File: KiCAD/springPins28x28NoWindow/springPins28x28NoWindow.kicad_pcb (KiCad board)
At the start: 2 copper layers, 28 x 28 mm, 26 parts, among them J1 CONN_02X06, J2 CONN_02X06

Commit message: update silk
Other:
- board text added: "c75b306"
- board text removed: "1ad7c5f"
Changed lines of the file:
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@@
     (effects (font (size 1 1) (thickness 0.25)))
   )
-  (gr_text 1ad7c5f (at 6.5 -12.5) (layer F.SilkS)
+  (gr_text c75b306 (at 6.5 -12.5) (layer F.SilkS)
     (effects (font (size 0.7 0.7) (thickness 0.175)))
   )

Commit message: wip commit
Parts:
- moved JP1 22.9 mm to (-5.50, -11.1)
- moved R1 13.7 mm to (5.00, 1.00), turned to 0 degrees
- moved J1 12.7 mm to (6.35, 6.35), turned to 90 degrees
- moved J2 10.5 mm to (6.35, -3.81), turned to 90 degrees
- moved G*** 10.2 mm to (0.00, 10.2), turned to 180 degrees
- turned L1 to 0 degrees
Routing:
- net /V5: track 6.21 -> 29.3 mm, vias 0 -> 1
- net /I5: track 6.40 -> 21.9 mm
- net /V3: track 7.00 -> 22.4 mm
- net /I7: track 9.29 -> 24.0 mm
- net /I3: track 7.20 -> 21.9 mm
- net /V1: track 7.80 -> 22.3 mm
- net /I2: track 7.99 -> 21.5 mm
- net /I1: track 7.99 -> 20.7 mm
- net /V2: track 7.80 -> 16.9 mm
- net /I6: track 6.40 -> 15.3 mm
- net /I4: track 7.20 -> 15.3 mm
- net /V7: track 15.2 -> 22.8 mm
- net /V6: track 6.21 -> 13.7 mm
- net /V4: track 7.00 -> 13.9 mm
- net /I8: track 9.29 -> 15.2 mm
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
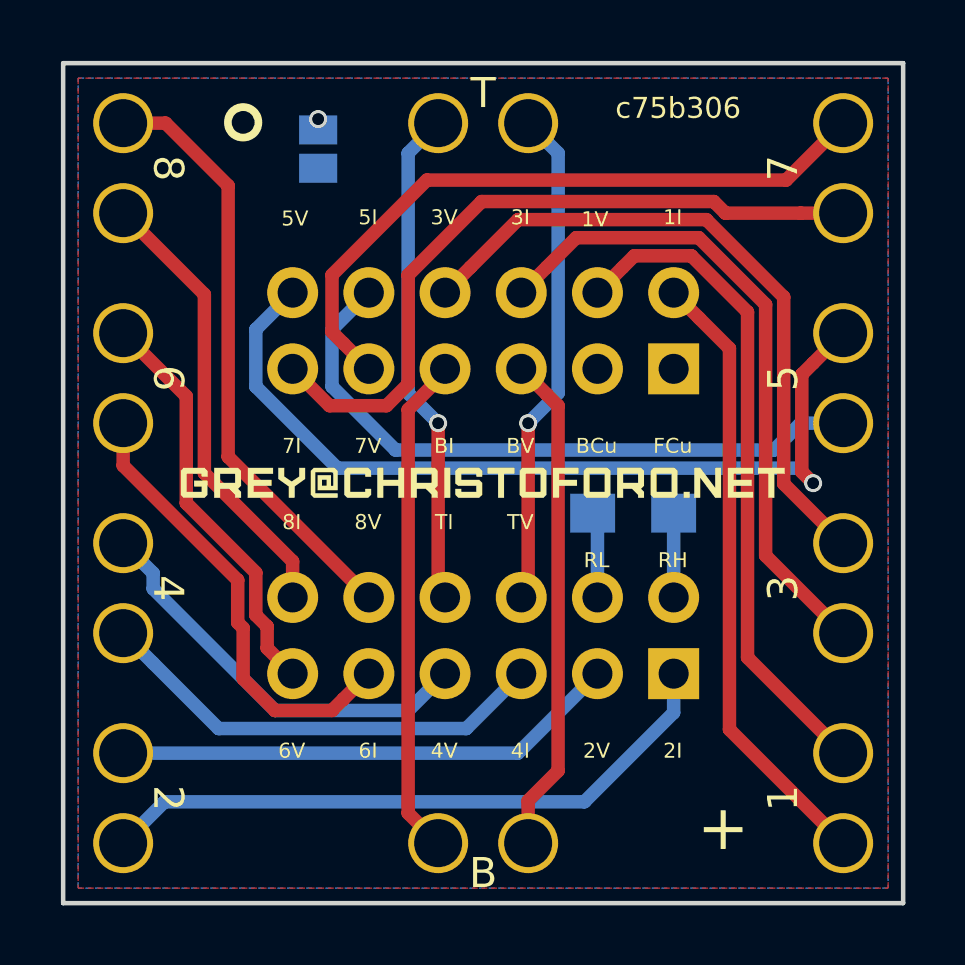
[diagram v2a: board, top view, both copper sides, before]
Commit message: go back to 28x28 layout
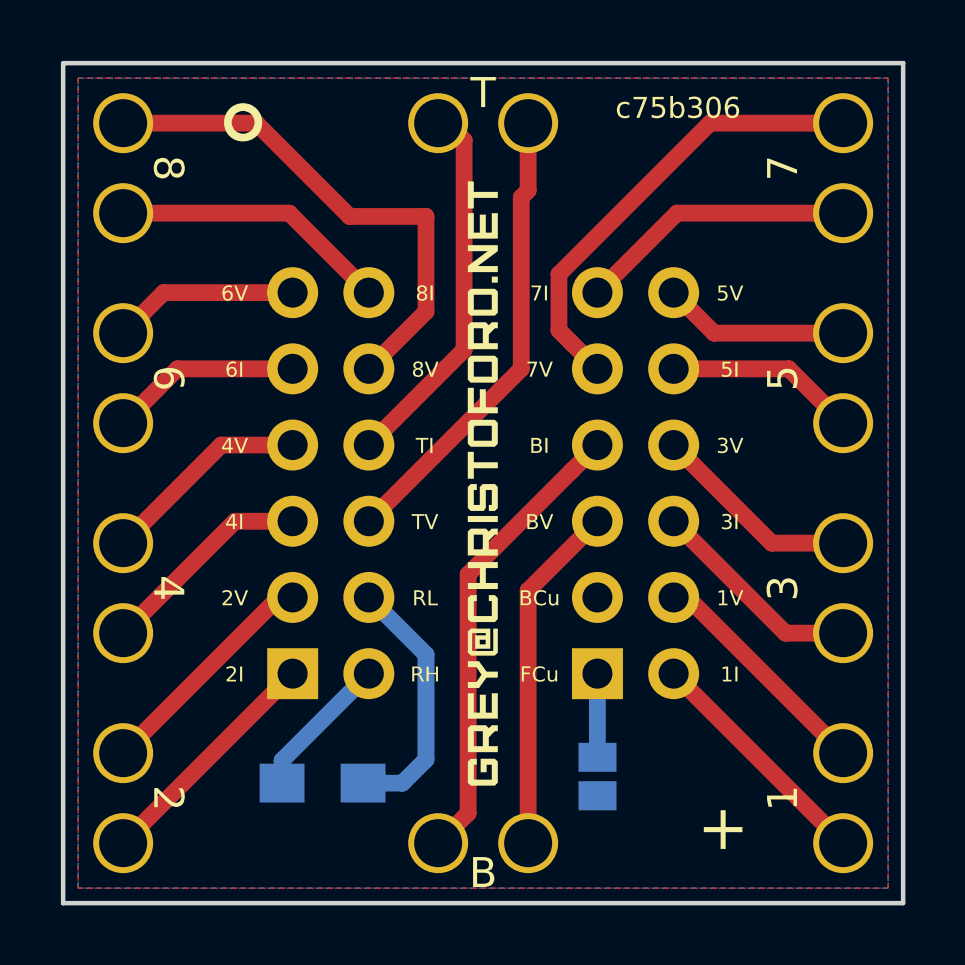
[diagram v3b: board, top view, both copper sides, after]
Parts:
- moved JP1 22.9 mm to (3.81, 9.78)
- moved R1 13.7 mm to (-5.35, 10.0), turned to 180 degrees
- moved J1 12.7 mm to (-6.35, 6.35), turned to 0 degrees
- moved J2 10.5 mm to (3.81, 6.35), turned to 0 degrees
- moved G*** 10.2 mm to (0.00, 0.00), turned to 270 degrees
- turned L1 to 90 degrees
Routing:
- net /V5: track 29.3 -> 6.21 mm, vias 1 -> 0
- net /I5: track 21.9 -> 6.40 mm
- net /V3: track 22.4 -> 7.00 mm
- net /I7: track 24.0 -> 9.29 mm
- net /I3: track 21.9 -> 7.20 mm
- net /V1: track 22.3 -> 7.80 mm
- net /I2: track 21.5 -> 7.99 mm
- net /I1: track 20.7 -> 7.99 mm
- net /V2: track 16.9 -> 7.80 mm
- net /I6: track 15.3 -> 6.40 mm
- net /I4: track 15.3 -> 7.20 mm
- net /V7: track 22.8 -> 15.2 mm
- net /V6: track 13.7 -> 6.21 mm
- net /V4: track 13.9 -> 7.00 mm
- net /I8: track 15.2 -> 9.29 mm
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
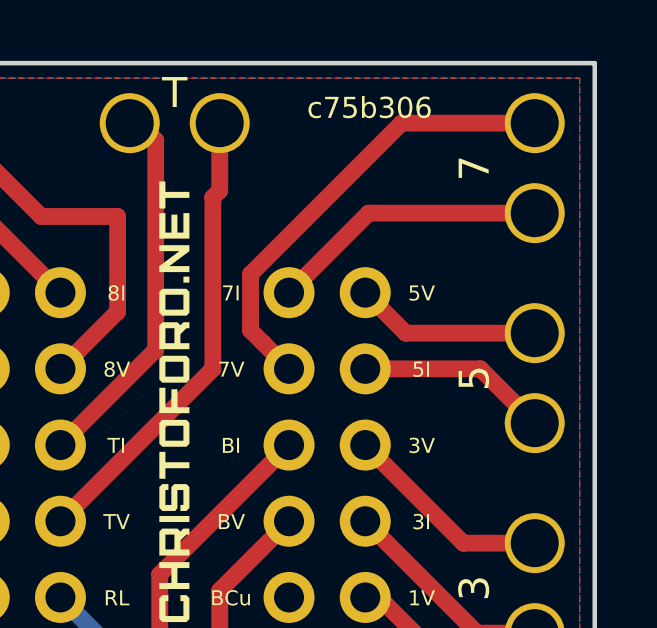
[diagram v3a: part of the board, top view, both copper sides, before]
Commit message: spruce up spring pin boards
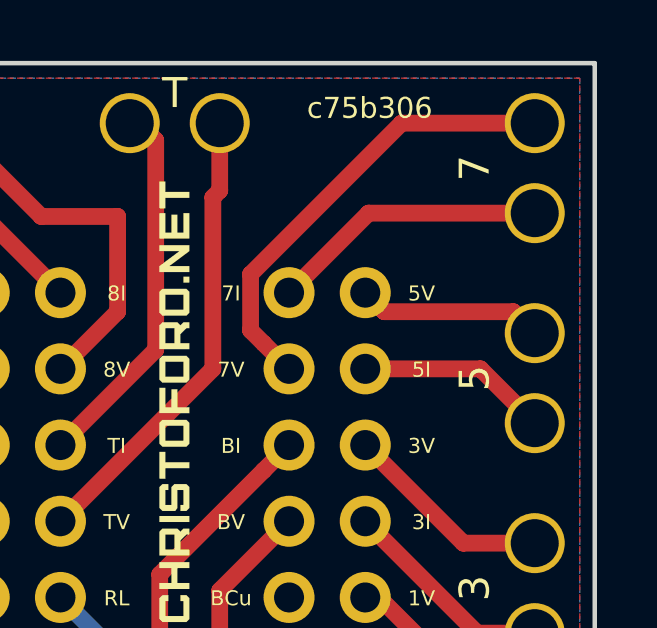
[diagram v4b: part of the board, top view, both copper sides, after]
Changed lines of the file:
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@@
-(kicad_pcb (version 20170123) (host pcbnew "(2017-09-19 revision 0083ce1bd)-master")
+(kicad_pcb (version 20171130) (host pcbnew "(5.0-dev-4060-g28f1209ce)")
   (general
     (thickness 1.6)
     (drawings 75)
-    (tracks 57)
+    (tracks 58)
     (zones 0)
     (modules 26)
@@
       (net 16 /I5))
     (model ${KIPRJMOD}/sharedLibs/myparts.3dshapes/S25-022+P25-4023.step
-      (at (xyz 0 0 0.2165354330708661))
+      (offset (xyz 0 0 5.499999917398286))
       (scale (xyz 1 1 1))
       (rotate (xyz -90 0 0))
@@
       (net 18 /V5))
     (model ${KIPRJMOD}/sharedLibs/myparts.3dshapes/S25-022+P25-4023.step
-      (at (xyz 0 0 0.2165354330708661))
+      (offset (xyz 0 0 5.499999917398286))
       (scale (xyz 1 1 1))
       (rotate (xyz -90 0 0))
@@
       (net 17 /I7))
     (model ${KIPRJMOD}/sharedLibs/myparts.3dshapes/S25-022+P25-4023.step
-      (at (xyz 0 0 0.2165354330708661))
+      (offset (xyz 0 0 5.499999917398286))
       (scale (xyz 1 1 1))
       (rotate (xyz -90 0 0))
@@
       (net 15 /V7))
     (model ${KIPRJMOD}/sharedLibs/myparts.3dshapes/S25-022+P25-4023.step
-      (at (xyz 0 0 0.2165354330708661))
+      (offset (xyz 0 0 5.499999917398286))
       (scale (xyz 1 1 1))
       (rotate (xyz -90 0 0))
@@
       (net 21 /VB))
     (model ${KIPRJMOD}/sharedLibs/myparts.3dshapes/S25-022+P25-4023.step
-      (at (xyz 0 0 0.2165354330708661))
+      (offset (xyz 0 0 5.499999917398286))
       (scale (xyz 1 1 1))
       (rotate (xyz -90 0 0))
@@
       (net 4 /VT))
     (model ${KIPRJMOD}/sharedLibs/myparts.3dshapes/S25-022+P25-4023.step
-      (at (xyz 0 0 0.2165354330708661))
+      (offset (xyz 0 0 5.499999917398286))
       (scale (xyz 1 1 1))
       (rotate (xyz -90 0 0))
@@
       (net 22 /IB))
     (model ${KIPRJMOD}/sharedLibs/myparts.3dshapes/S25-022+P25-4023.step
-      (at (xyz 0 0 0.2165354330708661))
+      (offset (xyz 0 0 5.499999917398286))
       (scale (xyz 1 1 1))
       (rotate (xyz -90 0 0))
@@
       (net 6 /IT))
     (model ${KIPRJMOD}/sharedLibs/myparts.3dshapes/S25-022+P25-4023.step
-      (at (xyz 0 0 0.2165354330708661))
+      (offset (xyz 0 0 5.499999917398286))
       (scale (xyz 1 1 1))
       (rotate (xyz -90 0 0))
@@
       (net 1 /I2))
     (model ${KIPRJMOD}/sharedLibs/myparts.3dshapes/S25-022+P25-4023.step
-      (at (xyz 0 0 0.2165354330708661))
+      (offset (xyz 0 0 5.499999917398286))
       (scale (xyz 1 1 1))
       (rotate (xyz -90 0 0))
@@
       (net 2 /V2))
     (model ${KIPRJMOD}/sharedLibs/myparts.3dshapes/S25-022+P25-4023.step
-      (at (xyz 0 0 0.2165354330708661))
+      (offset (xyz 0 0 5.499999917398286))
       (scale (xyz 1 1 1))
       (rotate (xyz -90 0 0))
@@
       (net 3 /I4))
     (model ${KIPRJMOD}/sharedLibs/myparts.3dshapes/S25-022+P25-4023.step
-      (at (xyz 0 0 0.2165354330708661))
+      (offset (xyz 0 0 5.499999917398286))
       (scale (xyz 1 1 1))
       (rotate (xyz -90 0 0))
@@
       (net 5 /V4))
     (model ${KIPRJMOD}/sharedLibs/myparts.3dshapes/S25-022+P25-4023.step
-      (at (xyz 0 0 0.2165354330708661))
+      (offset (xyz 0 0 5.499999917398286))
       (scale (xyz 1 1 1))
       (rotate (xyz -90 0 0))
@@
       (net 7 /I6))
     (model ${KIPRJMOD}/sharedLibs/myparts.3dshapes/S25-022+P25-4023.step
-      (at (xyz 0 0 0.2165354330708661))
+      (offset (xyz 0 0 5.499999917398286))
       (scale (xyz 1 1 1))
       (rotate (xyz -90 0 0))
@@
       (net 9 /V6))
     (model ${KIPRJMOD}/sharedLibs/myparts.3dshapes/S25-022+P25-4023.step
-      (at (xyz 0 0 0.2165354330708661))
+      (offset (xyz 0 0 5.499999917398286))
       (scale (xyz 1 1 1))
       (rotate (xyz -90 0 0))
@@
       (net 10 /I8))
     (model ${KIPRJMOD}/sharedLibs/myparts.3dshapes/S25-022+P25-4023.step
-      (at (xyz 0 0 0.2165354330708661))
+      (offset (xyz 0 0 5.499999917398286))
       (scale (xyz 1 1 1))
       (rotate (xyz -90 0 0))
@@
       (net 8 /V8))
     (model ${KIPRJMOD}/sharedLibs/myparts.3dshapes/S25-022+P25-4023.step
-      (at (xyz 0 0 0.2165354330708661))
+      (offset (xyz 0 0 5.499999917398286))
       (scale (xyz 1 1 1))
       (rotate (xyz -90 0 0))
@@
       (net 14 /V3))
     (model ${KIPRJMOD}/sharedLibs/myparts.3dshapes/S25-022+P25-4023.step
-      (at (xyz 0 0 0.2165354330708661))
+      (offset (xyz 0 0 5.499999917398286))
       (scale (xyz 1 1 1))
       (rotate (xyz -90 0 0))
@@
       (net 13 /I3))
     (model ${KIPRJMOD}/sharedLibs/myparts.3dshapes/S25-022+P25-4023.step
-      (at (xyz 0 0 0.2165354330708661))
+      (offset (xyz 0 0 5.499999917398286))
       (scale (xyz 1 1 1))
       (rotate (xyz -90 0 0))
@@
       (net 12 /V1))
     (model ${KIPRJMOD}/sharedLibs/myparts.3dshapes/S25-022+P25-4023.step
-      (at (xyz 0 0 0.2165354330708661))
+      (offset (xyz 0 0 5.499999917398286))
       (scale (xyz 1 1 1))
       (rotate (xyz -90 0 0))
@@
       (net 11 /I1))
     (model ${KIPRJMOD}/sharedLibs/myparts.3dshapes/S25-022+P25-4023.step
-      (at (xyz 0 0 0.2165354330708661))
+      (offset (xyz 0 0 5.499999917398286))
       (scale (xyz 1 1 1))
       (rotate (xyz -90 0 0))
@@
     (at 0 0 270)
     (fp_text reference G*** (at 0 4 270) (layer B.SilkS) hide
-      (effects (font (thickness 0.2)) (justify mirror))
+      (effects (font (size 1.524 1.524) (thickness 0.2)) (justify mirror))
     )
     (fp_text value value (at 0 -4 270) (layer B.SilkS) hide
-      (effects (font (thickness 0.2)) (justify mirror))
+      (effects (font (size 1.524 1.524) (thickness 0.2)) (justify mirror))
     )
     (fp_poly (pts (xy -0.030446 0.410336) (xy -0.128951 0.511719) (xy -0.828528 0.511719) (xy -0.927058 0.410336)
@@
     (at 0 0 90)
     (fp_text reference L1 (at 0 -4 90) (layer F.SilkS) hide
-      (effects (font (thickness 0.2)))
+      (effects (font (size 1.524 1.524) (thickness 0.2)))
     )
     (fp_text value GREY@CHRISTOFORO.NET (at 0 4 90) (layer F.SilkS) hide
-      (effects (font (thickness 0.2)))
+      (effects (font (size 1.524 1.524) (thickness 0.2)))
     )
     (fp_poly (pts (xy -0.030446 -0.410336) (xy -0.128951 -0.511719) (xy -0.828528 -0.511719) (xy -0.927058 -0.410336)
@@
   (segment (start 12 -9) (end 6.46 -9) (width 0.56) (layer F.Cu) (net 17))
   (segment (start 6.46 -9) (end 3.81 -6.35) (width 0.56) (layer F.Cu) (net 17))
-  (segment (start 12 -5) (end 7.7 -5) (width 0.56) (layer F.Cu) (net 18))
-  (segment (start 7.7 -5) (end 6.35 -6.35) (width 0.56) (layer F.Cu) (net 18))
+  (segment (start 11.285 -5.715) (end 6.985 -5.715) (width 0.56) (layer F.Cu) (net 18))
+  (segment (start 12 -5) (end 11.285 -5.715) (width 0.56) (layer F.Cu) (net 18))
+  (segment (start 6.985 -5.715) (end 6.35 -6.35) (width 0.56) (layer F.Cu) (net 18))
   (segment (start -6.7 10) (end -6.7 9.24) (width 0.56) (layer B.Cu) (net 19))
   (segment (start -6.7 9.24) (end -3.81 6.35) (width 0.56) (layer B.Cu) (net 19))

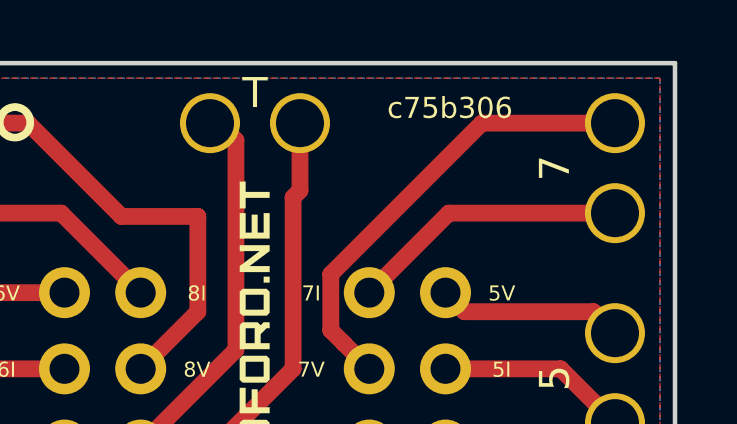
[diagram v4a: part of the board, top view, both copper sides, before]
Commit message: move arduino headers into myparts
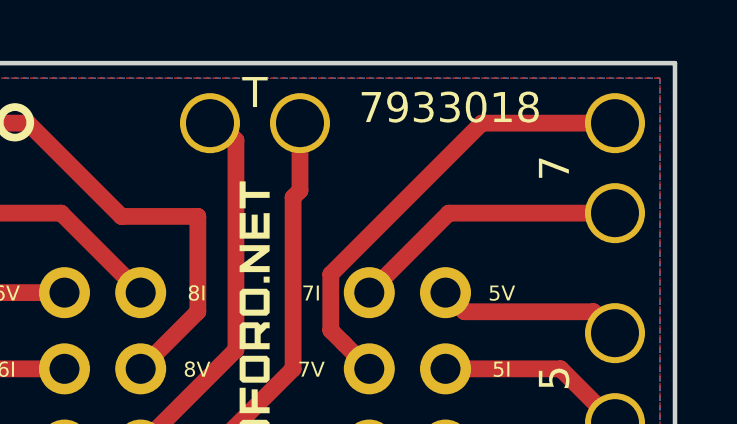
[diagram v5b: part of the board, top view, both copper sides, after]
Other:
- board text added: "7933018"
- board text removed: "c75b306"
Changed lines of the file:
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@@
     (effects (font (size 1 1) (thickness 0.25)))
   )
-  (gr_text c75b306 (at 6.5 -12.5) (layer F.SilkS)
-    (effects (font (size 0.7 0.7) (thickness 0.175)))
+  (gr_text 7933018 (at 6.5 -12.5) (layer F.SilkS)
+    (effects (font (size 1 1) (thickness 0.175)))
   )
   (gr_text B (at 0 13) (layer F.SilkS)

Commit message: update silk
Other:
- board text added: "3ec2e93"
- board text removed: "7933018"
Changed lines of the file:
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@@
     (effects (font (size 1 1) (thickness 0.25)))
   )
-  (gr_text 7933018 (at 6.5 -12.5) (layer F.SilkS)
+  (gr_text 3ec2e93 (at 6.5 -12.5) (layer F.SilkS)
     (effects (font (size 1 1) (thickness 0.175)))
   )

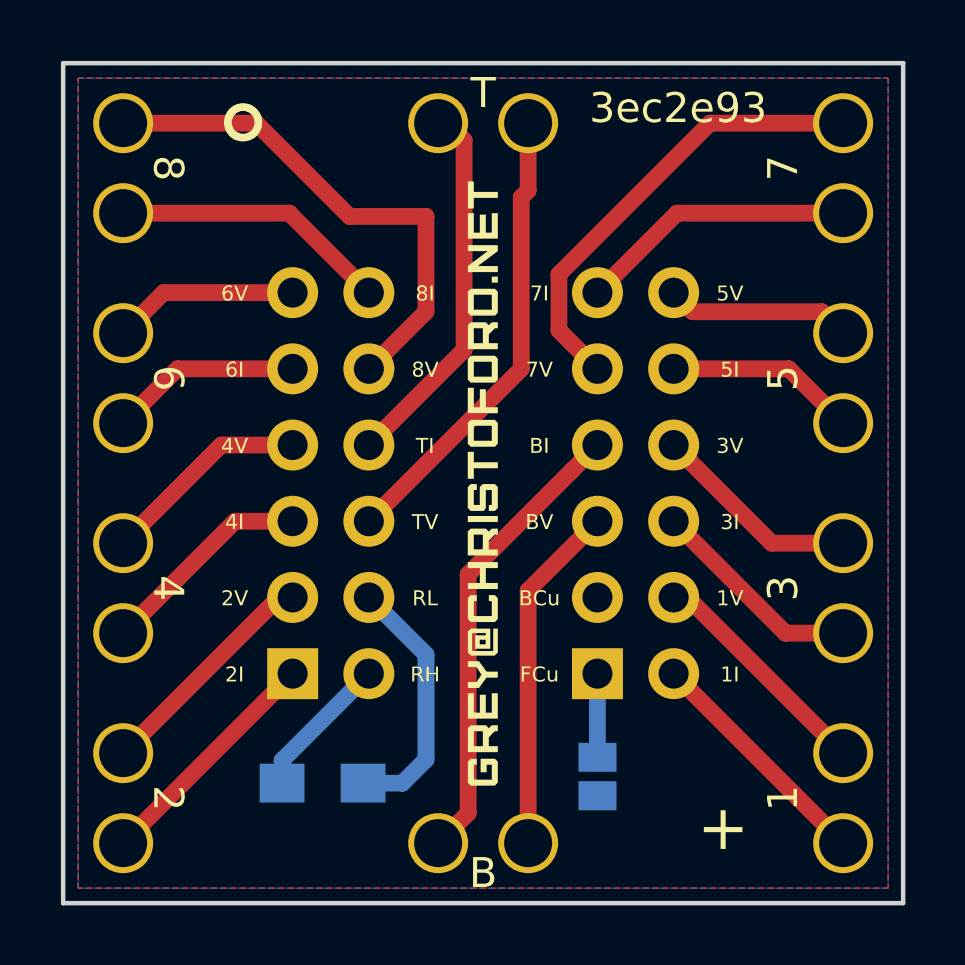
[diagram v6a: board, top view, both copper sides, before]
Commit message: starting on ethercat board pin boards rotated base1x zones fixed
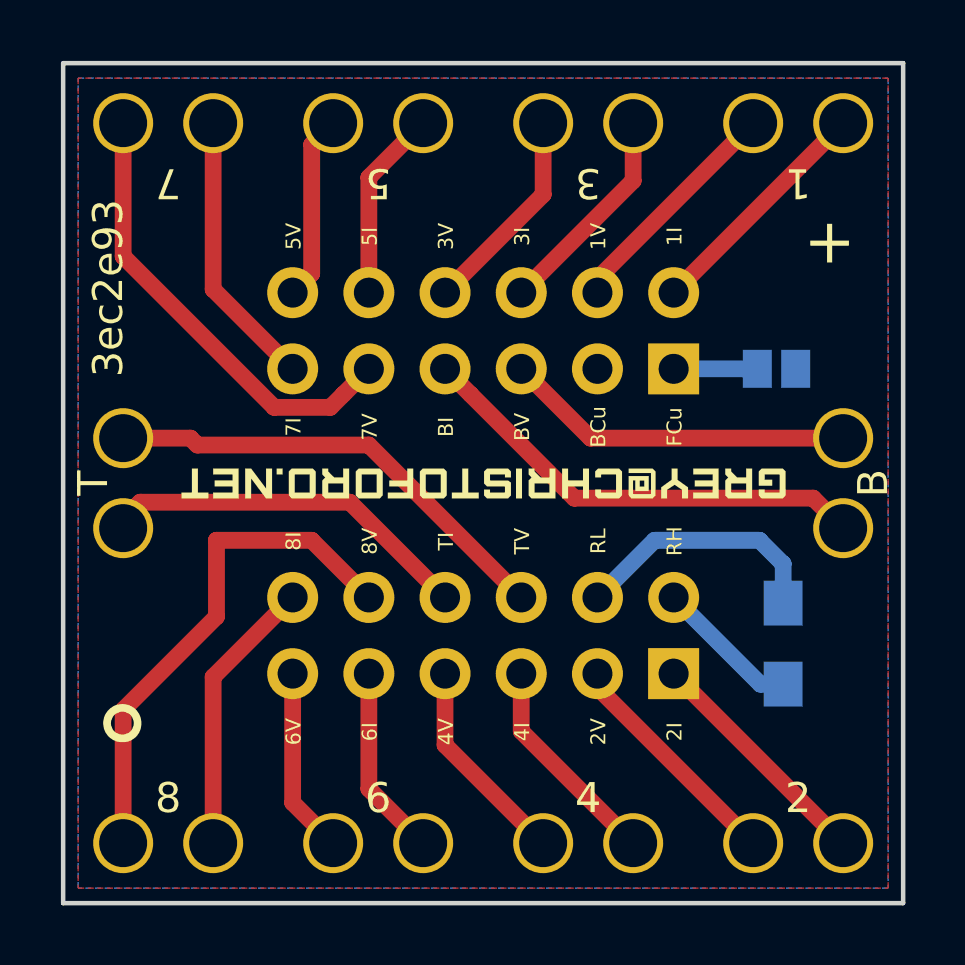
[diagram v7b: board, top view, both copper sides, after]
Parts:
- moved TP1 24.0 mm to (-12.0, 12.0), turned to 90 degrees
- moved TP13 24.0 mm to (-12.0, -12.0), turned to 90 degrees
- moved TP20 24.0 mm to (12.0, -12.0), turned to 90 degrees
- moved TP8 24.0 mm to (12.0, 12.0), turned to 90 degrees
- moved TP14 21.2 mm to (-9.00, -12.0), turned to 90 degrees
- moved TP19 21.2 mm to (9.00, -12.0), turned to 90 degrees
- moved TP2 21.2 mm to (-9.00, 12.0), turned to 90 degrees
- moved TP7 21.2 mm to (9.00, 12.0), turned to 90 degrees
- moved TP15 18.4 mm to (-5.00, -12.0), turned to 90 degrees
- moved TP18 18.4 mm to (5.00, -12.0), turned to 90 degrees
- moved TP3 18.4 mm to (-5.00, 12.0), turned to 90 degrees
- moved TP6 18.4 mm to (5.00, 12.0), turned to 90 degrees
- moved TP16 17.2 mm to (-2.00, -12.0), turned to 90 degrees
- moved TP17 17.2 mm to (2.00, -12.0), turned to 90 degrees
- moved TP4 17.2 mm to (-2.00, 12.0), turned to 90 degrees
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
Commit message: update silk
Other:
- board text added: "20b2bb8"
- board text removed: "3ec2e93"
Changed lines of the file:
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@@
-(kicad_pcb (version 20171130) (host pcbnew "(5.0-dev-4085-g9241a399a)")
+(kicad_pcb (version 20171130) (host pcbnew "(5.0.0-rc2-dev-44-gde6b32d23)")
   (general
     (thickness 1.6)
@@
       (usegerberattributes true)
       (usegerberadvancedattributes true)
-      (creategerberjobfile true)
+      (creategerberjobfile false)
       (excludeedgelayer true)
       (linewidth 0.150000)
@@
     (effects (font (size 1 1) (thickness 0.25)))
   )
-  (gr_text 3ec2e93 (at -12.5 -6.5 90) (layer F.SilkS)
+  (gr_text 20b2bb8 (at -12.5 -6.5 90) (layer F.SilkS)
     (effects (font (size 1 1) (thickness 0.175)))
   )
